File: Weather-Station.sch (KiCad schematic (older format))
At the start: 53 parts

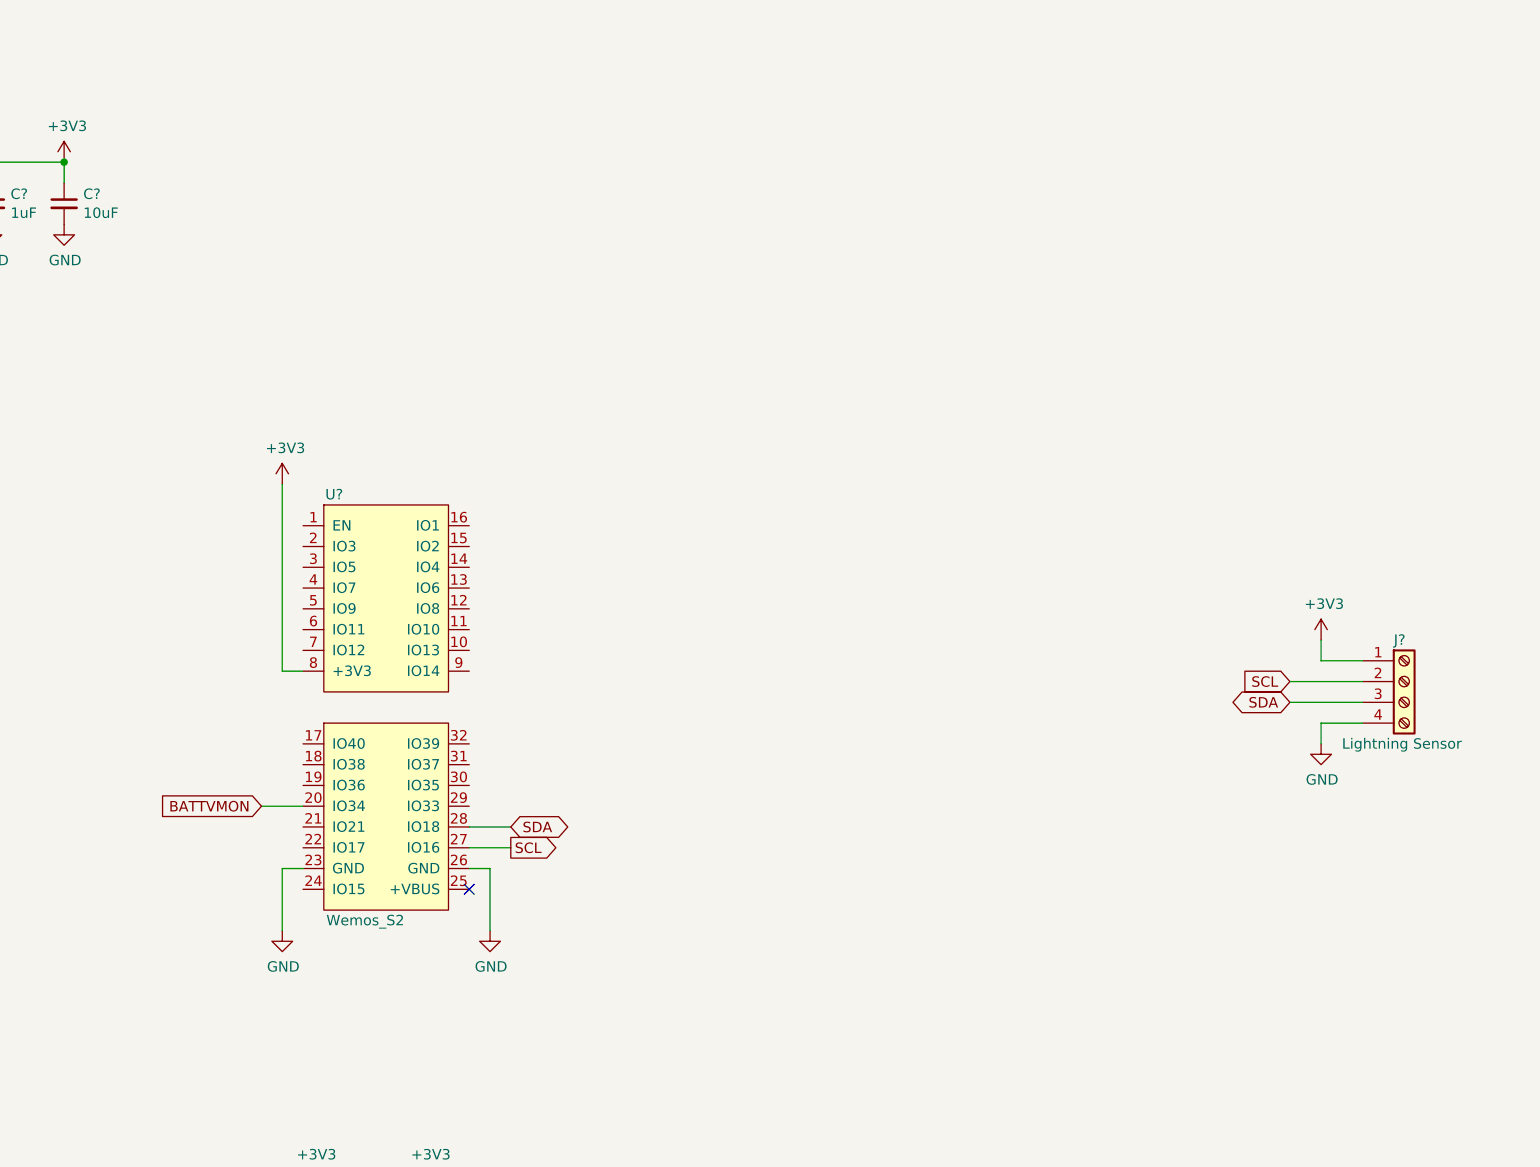
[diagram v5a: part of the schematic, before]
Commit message: Added 3.3V TTL for rain gauge and start of photoelectric circuit
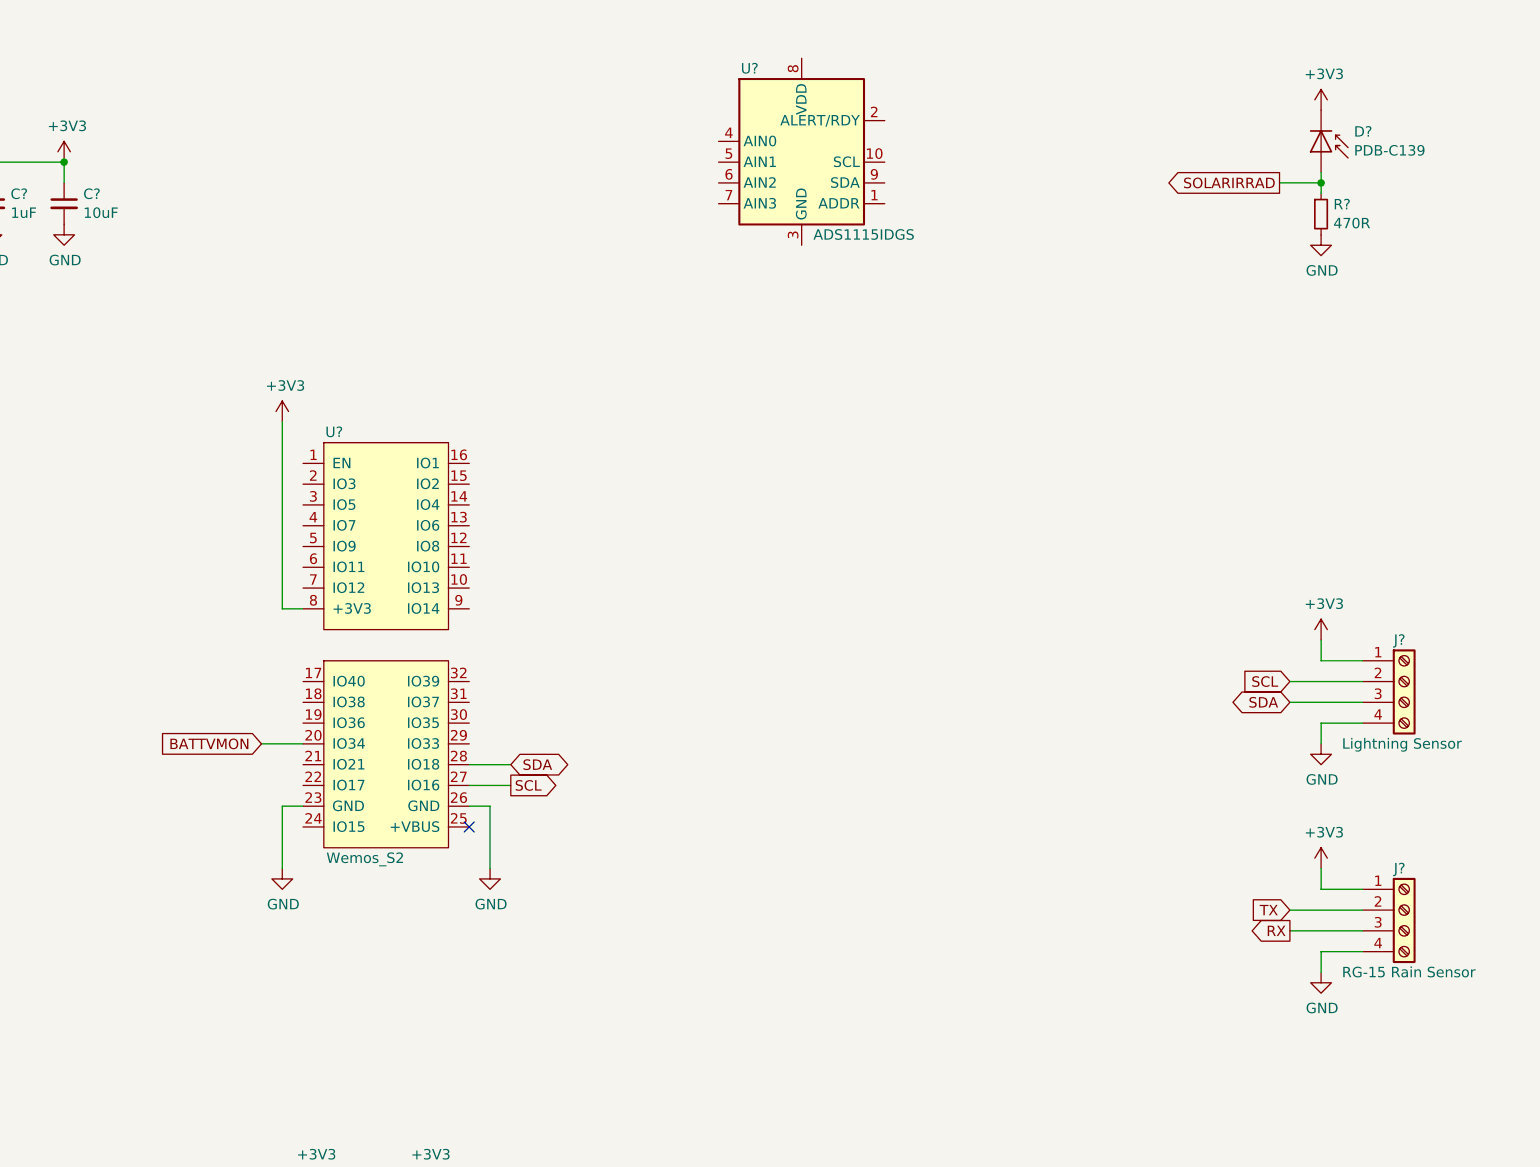
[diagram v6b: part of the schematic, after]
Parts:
- added D?: PDB-C139, symbol Device:D_Photo
- added J?: RG-15 Rain Sensor, TerminalBlock:TerminalBlock_bornier-4_P5.08mm, symbol Connector:Screw_Terminal_01x04
- added R?: 470R, Resistor_SMD:R_0805_2012Metric, symbol Device:R_Small
- added U?: ADS1115IDGS, Package_SO:TSSOP-10_3x3mm_P0.5mm, symbol Analog_ADC:ADS1115IDGS
- J?: footprint (none) -> TerminalBlock:TerminalBlock_bornier-4_P5.08mm
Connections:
- net +3V3: now also D?.1 (K), J?.1 (Pin_1)
- net GND: now also J?.4 (Pin_4), R?.2
- new net RX: J?.3 (Pin_3)
- new net SOLARIRRAD: D?.2 (A), R?.1
- new net TX: J?.2 (Pin_2)
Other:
- moved on the sheet: U?
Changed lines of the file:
@@
 L WemosS2:Wemos_S2 U?
 U 1 1 618E7311
-P 9400 3500
-F 0 "U?" H 9450 3550 50  0000 C CNN
-F 1 "Wemos_S2" H 9600 1500 50  0000 C CNN
-F 2 "" H 9400 3450 50  0001 C CNN
-F 3 "" H 9400 3450 50  0001 C CNN
-	1    9400 3500
+P 9400 3200
+F 0 "U?" H 9450 3250 50  0000 C CNN
+F 1 "Wemos_S2" H 9600 1200 50  0000 C CNN
+F 2 "" H 9400 3150 50  0001 C CNN
+F 3 "" H 9400 3150 50  0001 C CNN
+	1    9400 3200
 	1    0    0    -1
 $EndComp
@@
 L power:+3V3 #PWR?
 U 1 1 61A53F67
-P 9200 3400
-F 0 "#PWR?" H 9200 3250 50  0001 C CNN
-F 1 "+3V3" H 9215 3573 50  0000 C CNN
-F 2 "" H 9200 3400 50  0001 C CNN
-F 3 "" H 9200 3400 50  0001 C CNN
-	1    9200 3400
-	1    0    0    -1
-$EndComp
-NoConn ~ 10100 5350
-Wire Wire Line
-	9200 3400 9200 4300
-Wire Wire Line
-	9200 4300 9300 4300
+P 9200 3100
+F 0 "#PWR?" H 9200 2950 50  0001 C CNN
+F 1 "+3V3" H 9215 3273 50  0000 C CNN
+F 2 "" H 9200 3100 50  0001 C CNN
+F 3 "" H 9200 3100 50  0001 C CNN
+	1    9200 3100
+	1    0    0    -1
+$EndComp
+NoConn ~ 10100 5050
+Wire Wire Line
+	9200 3100 9200 4000
+Wire Wire Line
+	9200 4000 9300 4000
 $Comp
 L power:GND #PWR?
 U 1 1 61A64F93
-P 9200 5550
-F 0 "#PWR?" H 9200 5300 50  0001 C CNN
-F 1 "GND" H 9205 5377 50  0000 C CNN
-F 2 "" H 9200 5550 50  0001 C CNN
-F 3 "" H 9200 5550 50  0001 C CNN
-	1    9200 5550
+P 9200 5250
+F 0 "#PWR?" H 9200 5000 50  0001 C CNN
+F 1 "GND" H 9205 5077 50  0000 C CNN
+F 2 "" H 9200 5250 50  0001 C CNN
+F 3 "" H 9200 5250 50  0001 C CNN
+	1    9200 5250
 	1    0    0    -1
 $EndComp
@@
 L power:GND #PWR?
 U 1 1 61A657A2
-P 10200 5550
-F 0 "#PWR?" H 10200 5300 50  0001 C CNN
-F 1 "GND" H 10205 5377 50  0000 C CNN
-F 2 "" H 10200 5550 50  0001 C CNN
-F 3 "" H 10200 5550 50  0001 C CNN
-	1    10200 5550
-	1    0    0    -1
-$EndComp
-Wire Wire Line
-	10200 5550 10200 5250
-Wire Wire Line
-	10200 5250 10100 5250
-Wire Wire Line
-	9200 5550 9200 5250
-Wire Wire Line
-	9200 5250 9300 5250
+P 10200 5250
+F 0 "#PWR?" H 10200 5000 50  0001 C CNN
+F 1 "GND" H 10205 5077 50  0000 C CNN
+F 2 "" H 10200 5250 50  0001 C CNN
+F 3 "" H 10200 5250 50  0001 C CNN
+	1    10200 5250
+	1    0    0    -1
+$EndComp
+Wire Wire Line
+	10200 5250 10200 4950
+Wire Wire Line
+	10200 4950 10100 4950
+Wire Wire Line
+	9200 5250 9200 4950
+Wire Wire Line
+	9200 4950 9300 4950
 Text Notes 4500 3350 0    50   ~ 0
 Vhigh = 4.4V approx.\nVlow = 3.375V approx.
-Text GLabel 9100 4950 0    50   Input ~ 0
+Text GLabel 9100 4650 0    50   Input ~ 0
 BATTVMON
 Wire Wire Line
-	9300 4950 9100 4950
+	9300 4650 9100 4650
 Text GLabel 6000 2950 2    50   Output ~ 0
 BATTVMON
@@
 Wire Wire Line
 	5800 2950 6000 2950
-Text GLabel 10300 5050 2    50   BiDi ~ 0
+Text GLabel 10300 4750 2    50   BiDi ~ 0
 SDA
 Wire Wire Line
-	10300 5050 10100 5050
-Text GLabel 10300 5150 2    50   Output ~ 0
+	10300 4750 10100 4750
+Text GLabel 10300 4850 2    50   Output ~ 0
 SCL
 Wire Wire Line
-	10300 5150 10100 5150
+	10300 4850 10100 4850
 Text GLabel 14050 4450 0    50   BiDi ~ 0
 SDA
@@
 F 0 "J?" H 14550 4550 50  0000 L CNN
 F 1 "Lightning Sensor" H 14300 4050 50  0000 L CNN
-F 2 "" H 14600 4350 50  0001 C CNN
+F 2 "TerminalBlock:TerminalBlock_bornier-4_P5.08mm" H 14600 4350 50  0001 C CNN
 F 3 "~" H 14600 4350 50  0001 C CNN
 	1    14600 4350
@@
 Wire Wire Line
 	14200 4550 14200 4650
+$Comp
+L Device:D_Photo D?
+U 1 1 619F7CEC
+P 14200 1800
+F 0 "D?" V 14104 1958 50  0000 L CNN
+F 1 "PDB-C139" V 14195 1958 50  0000 L CNN
+F 2 "" H 14150 1800 50  0001 C CNN
+F 3 "~" H 14150 1800 50  0001 C CNN
+	1    14200 1800
+	0    1    1    0
+$EndComp
+$Comp
+L Device:R_Small R?
+U 1 1 619F8699
+P 14200 2100
+F 0 "R?" H 14259 2146 50  0000 L CNN
+F 1 "470R" H 14259 2055 50  0000 L CNN
+F 2 "Resistor_SMD:R_0805_2012Metric" H 14200 2100 50  0001 C CNN
+F 3 "~" H 14200 2100 50  0001 C CNN
+	1    14200 2100
+	1    0    0    -1
+$EndComp
+$Comp
+L power:GND #PWR?
+U 1 1 619F9126
+P 14200 2200
+F 0 "#PWR?" H 14200 1950 50  0001 C CNN
+F 1 "GND" H 14205 2027 50  0000 C CNN
+F 2 "" H 14200 2200 50  0001 C CNN
+F 3 "" H 14200 2200 50  0001 C CNN
+	1    14200 2200
+	1    0    0    -1
+$EndComp
+$Comp
+L power:+3V3 #PWR?
+U 1 1 619F9743
+P 14200 1600
+F 0 "#PWR?" H 14200 1450 50  0001 C CNN
+F 1 "+3V3" H 14215 1773 50  0000 C CNN
+F 2 "" H 14200 1600 50  0001 C CNN
+F 3 "" H 14200 1600 50  0001 C CNN
+	1    14200 1600
+	1    0    0    -1
+$EndComp
+Text GLabel 14000 1950 0    50   Output ~ 0
+SOLARIRRAD
+Wire Wire Line
+	14200 2000 14200 1950
+Wire Wire Line
+	14000 1950 14200 1950
+Connection ~ 14200 1950
+Wire Wire Line
+	14200 1950 14200 1900
+$Comp
+L Analog_ADC:ADS1115IDGS U?
+U 1 1 619F853B
+P 11700 1850
+F 0 "U?" H 11450 2300 50  0000 C CNN
+F 1 "ADS1115IDGS" H 12000 1500 50  0000 C CNN
+F 2 "Package_SO:TSSOP-10_3x3mm_P0.5mm" H 11700 1350 50  0001 C CNN
+F 3 "http://www.ti.com/lit/ds/symlink/ads1113.pdf" H 11650 950 50  0001 C CNN
+	1    11700 1850
+	1    0    0    -1
+$EndComp
+$Comp
+L power:GND #PWR?
+U 1 1 61A0DCA6
+P 14200 5750
+F 0 "#PWR?" H 14200 5500 50  0001 C CNN
+F 1 "GND" H 14205 5577 50  0000 C CNN
+F 2 "" H 14200 5750 50  0001 C CNN
+F 3 "" H 14200 5750 50  0001 C CNN
+	1    14200 5750
+	1    0    0    -1
+$EndComp
+$Comp
+L power:+3V3 #PWR?
+U 1 1 61A0DCAC
+P 14200 5250
+F 0 "#PWR?" H 14200 5100 50  0001 C CNN
+F 1 "+3V3" H 14215 5423 50  0000 C CNN
+F 2 "" H 14200 5250 50  0001 C CNN
+F 3 "" H 14200 5250 50  0001 C CNN
+	1    14200 5250
+	1    0    0    -1
+$EndComp
+$Comp
+L Connector:Screw_Terminal_01x04 J?
+U 1 1 61A0DCB2
+P 14600 5450
+F 0 "J?" H 14550 5650 50  0000 L CNN
+F 1 "RG-15 Rain Sensor" H 14300 5150 50  0000 L CNN
+F 2 "TerminalBlock:TerminalBlock_bornier-4_P5.08mm" H 14600 5450 50  0001 C CNN
+F 3 "~" H 14600 5450 50  0001 C CNN
+	1    14600 5450
+	1    0    0    -1
+$EndComp
+Wire Wire Line
+	14400 5350 14200 5350
+Wire Wire Line
+	14200 5350 14200 5250
+Wire Wire Line
+	14400 5450 14050 5450
+Wire Wire Line
+	14050 5550 14400 5550
+Wire Wire Line
+	14400 5650 14200 5650
+Wire Wire Line
+	14200 5650 14200 5750
+Text GLabel 14050 5450 0    50   Input ~ 0
+TX
+Text GLabel 14050 5550 0    50   Output ~ 0
+RX
 $EndSCHEMATC
